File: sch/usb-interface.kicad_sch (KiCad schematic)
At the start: 4 parts, among them IC1 USB2244I-AEZG-06

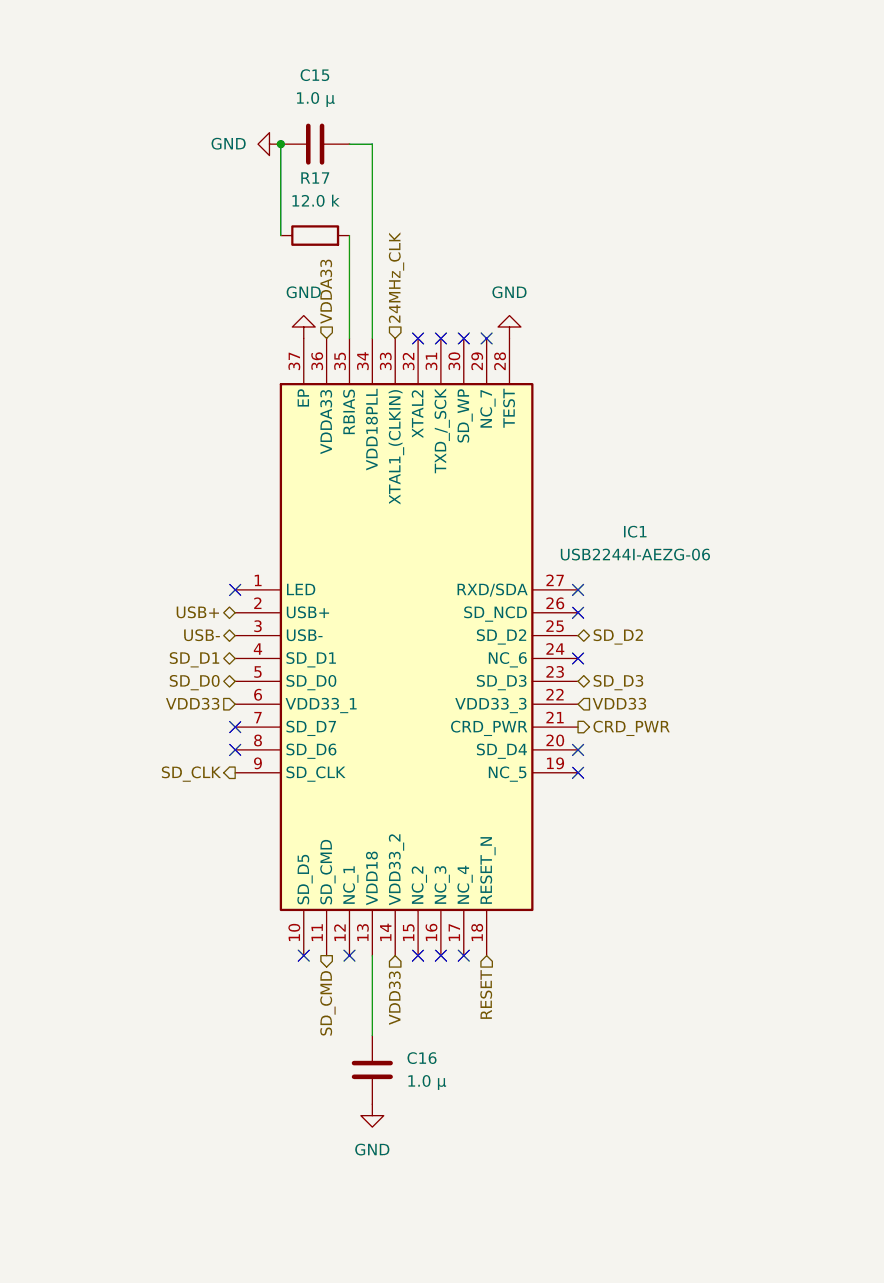
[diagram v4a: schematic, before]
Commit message: added ports to powersupply
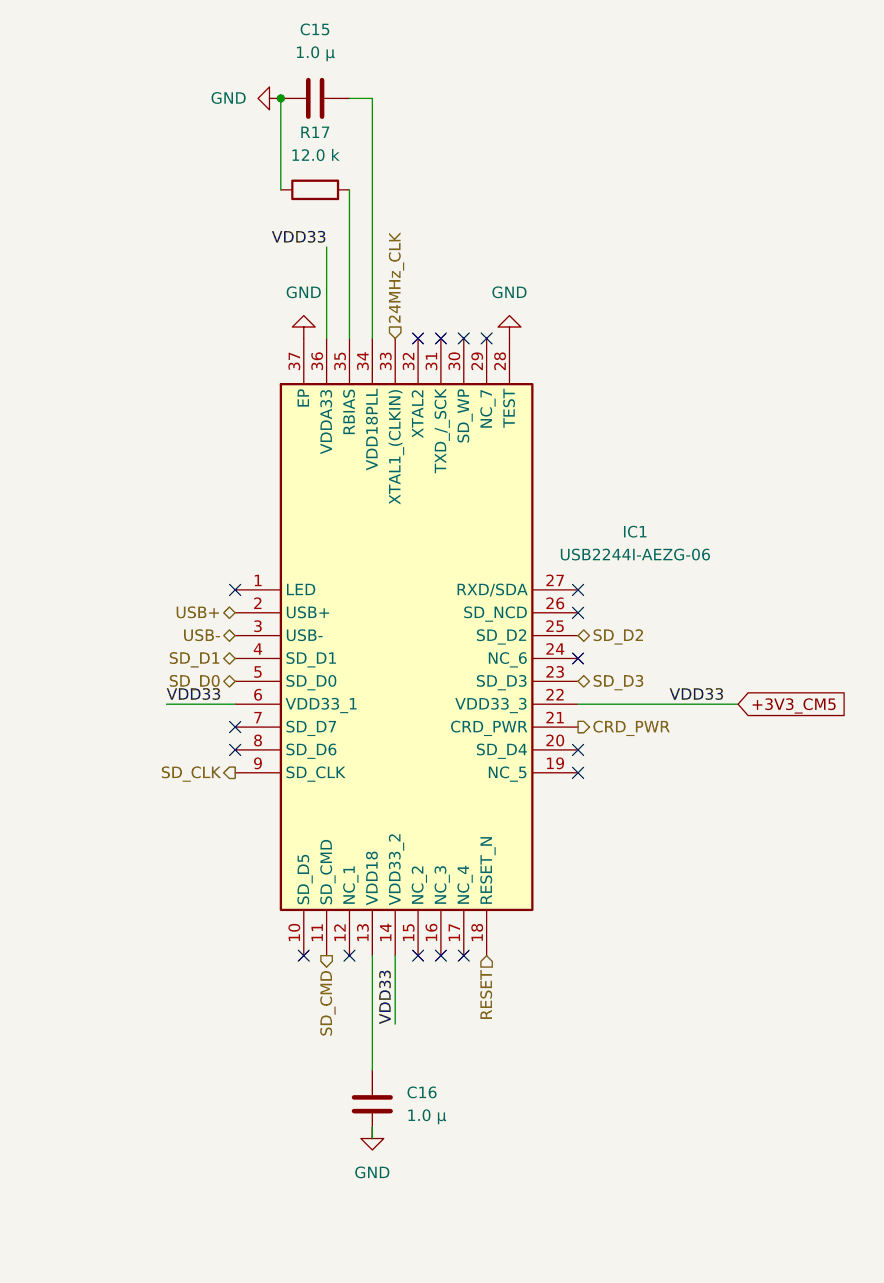
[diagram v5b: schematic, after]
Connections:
- net VDDA33 is gone; now on net +3V3_CM5: IC1.36 (VDDA33)
- net VDD33 renamed +3V3_CM5
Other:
- moved on the sheet: C15, C16, R17

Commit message: work pcb about 70 percent
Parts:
- added C21, C22, C23, C24: 4.7uF, Capacitor_SMD:C_0603_1608Metric, symbol Device:C_Small
- IC1: footprint QFN50P600X600X90-37N-D -> Package_DFN_QFN:QFN-36-1EP_6x6mm_P0.5mm_EP4.1x4.1mm_ThermalVias
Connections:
- net +3V3_CM5: now also C21.1, C22.1, C23.1, C24.2
- net GND: now also C21.2, C22.2, C23.2, C24.1
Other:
- moved on the sheet: C15, C16, R17

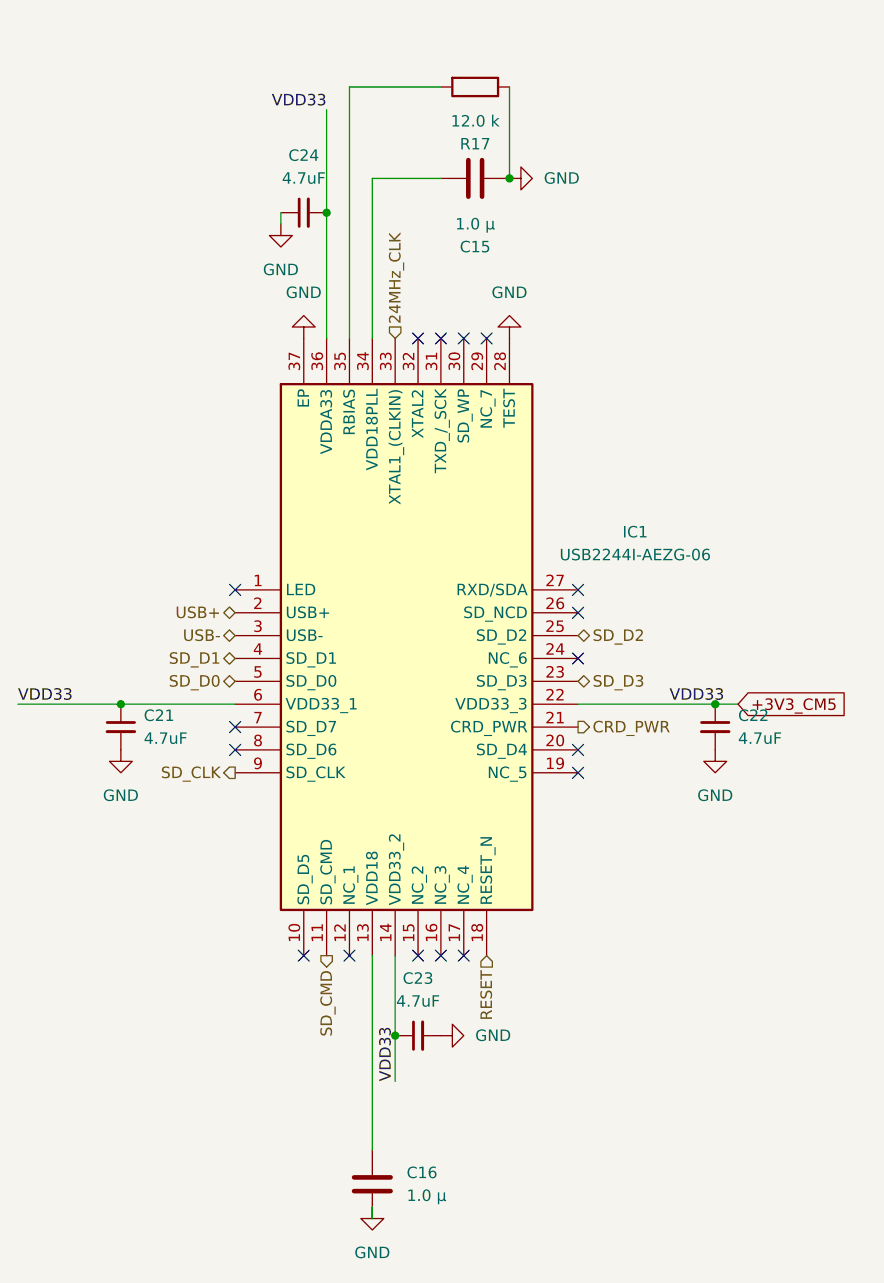
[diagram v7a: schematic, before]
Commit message: Endret nummereringer komponenter
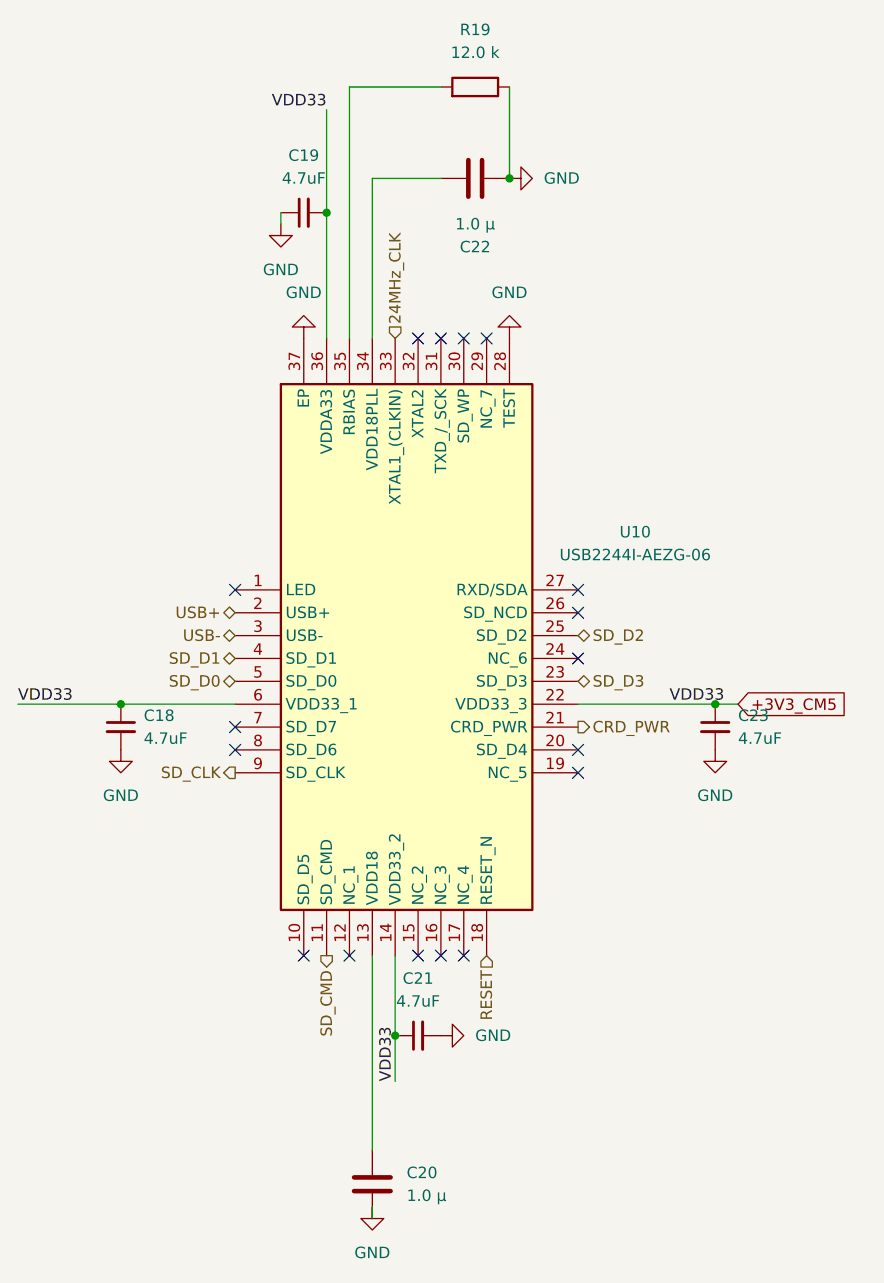
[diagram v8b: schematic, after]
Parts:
- renumbered C21 to C18, C24 to C19, C16 to C20, C23 to C21, C15 to C22, C22 to C23, R17 to R19, IC1 to U10
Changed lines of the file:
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@@
 		(dnp no)
 		(fields_autoplaced yes)
-		(property "Reference" "#PWR037"
+		(property "Reference" "#PWR066"
 			(at 55.88 109.22 0)
 			(effects
@@
 			(project "audiograb"
 				(path "/c46c2311-6d4b-411d-b012-c7730eac136d/53f9c81a-1433-4854-9dfc-932cf29aee40"
-					(reference "#PWR037")
+					(reference "#PWR066")
 					(unit 1)
 				)
@@
 		(dnp no)
 		(fields_autoplaced yes)
-		(property "Reference" "C22"
+		(property "Reference" "C23"
 			(at 124.46 99.0662 0)
 			(effects
@@
 			(project "audiograb"
 				(path "/c46c2311-6d4b-411d-b012-c7730eac136d/53f9c81a-1433-4854-9dfc-932cf29aee40"
-					(reference "C22")
+					(reference "C23")
 					(unit 1)
 				)
@@
 		(dnp no)
 		(fields_autoplaced yes)
-		(property "Reference" "C21"
+		(property "Reference" "C18"
 			(at 58.42 99.0662 0)
 			(effects
@@
 			(project "audiograb"
 				(path "/c46c2311-6d4b-411d-b012-c7730eac136d/53f9c81a-1433-4854-9dfc-932cf29aee40"
-					(reference "C21")
+					(reference "C18")
 					(unit 1)
 				)
@@
 		(dnp no)
 		(fields_autoplaced yes)
-		(property "Reference" "#PWR060"
+		(property "Reference" "#PWR069"
 			(at 83.82 160.02 0)
 			(effects
@@
 			(project "audiograb"
 				(path "/c46c2311-6d4b-411d-b012-c7730eac136d/53f9c81a-1433-4854-9dfc-932cf29aee40"
-					(reference "#PWR060")
+					(reference "#PWR069")
 					(unit 1)
 				)
@@
 		(dnp no)
 		(fields_autoplaced yes)
-		(property "Reference" "#PWR032"
+		(property "Reference" "#PWR070"
 			(at 97.79 134.62 0)
 			(effects
@@
 			(project "audiograb"
 				(path "/c46c2311-6d4b-411d-b012-c7730eac136d/53f9c81a-1433-4854-9dfc-932cf29aee40"
-					(reference "#PWR032")
+					(reference "#PWR070")
 					(unit 1)
 				)
@@
 		(dnp no)
 		(fields_autoplaced yes)
-		(property "Reference" "#PWR069"
+		(property "Reference" "#PWR067"
 			(at 73.66 50.8 0)
 			(effects
@@
 			(project "audiograb"
 				(path "/c46c2311-6d4b-411d-b012-c7730eac136d/53f9c81a-1433-4854-9dfc-932cf29aee40"
-					(reference "#PWR069")
+					(reference "#PWR067")
 					(unit 1)
 				)
@@
 		(dnp no)
 		(fields_autoplaced yes)
-		(property "Reference" "C15"
+		(property "Reference" "C22"
 			(at 95.25 46.99 90)
 			(effects
@@
 			(project "audiograb"
 				(path "/c46c2311-6d4b-411d-b012-c7730eac136d/53f9c81a-1433-4854-9dfc-932cf29aee40"
-					(reference "C15")
+					(reference "C22")
 					(unit 1)
 				)
@@
 		(dnp no)
 		(fields_autoplaced yes)
-		(property "Reference" "C24"
+		(property "Reference" "C19"
 			(at 76.2063 36.83 90)
 			(effects
@@
 			(project "audiograb"
 				(path "/c46c2311-6d4b-411d-b012-c7730eac136d/53f9c81a-1433-4854-9dfc-932cf29aee40"
-					(reference "C24")
+					(reference "C19")
 					(unit 1)
 				)
@@
 		(dnp no)
 		(fields_autoplaced yes)
-		(property "Reference" "C23"
+		(property "Reference" "C21"
 			(at 88.9063 128.27 90)
 			(effects
@@
 			(project "audiograb"
 				(path "/c46c2311-6d4b-411d-b012-c7730eac136d/53f9c81a-1433-4854-9dfc-932cf29aee40"
-					(reference "C23")
+					(reference "C21")
 					(unit 1)
 				)
@@
 		(dnp no)
 		(fields_autoplaced yes)
-		(property "Reference" "C16"
+		(property "Reference" "C20"
 			(at 87.63 149.8599 0)
 			(effects
@@
 			(project "audiograb"
 				(path "/c46c2311-6d4b-411d-b012-c7730eac136d/53f9c81a-1433-4854-9dfc-932cf29aee40"
-					(reference "C16")
+					(reference "C20")
 					(unit 1)
 				)
@@
 		(lib_id "Device:R")
 		(at 95.25 29.21 270)
-		(unit 1)
-		(exclude_from_sim no)
-		(in_bom yes)
-		(on_board yes)
-		(dnp no)
-		(fields_autoplaced yes)
-		(property "Reference" "R17"
-			(at 95.25 35.56 90)
+		(mirror x)
+		(unit 1)
+		(exclude_from_sim no)
+		(in_bom yes)
+		(on_board yes)
+		(dnp no)
+		(property "Reference" "R19"
+			(at 95.25 22.86 90)
 			(effects
 				(font
@@
 		)
 		(property "Value" "12.0 k"
-			(at 95.25 33.02 90)
+			(at 95.25 25.4 90)
 			(effects
 				(font
@@
 		)
 		(property "Footprint" "Resistor_SMD:R_0603_1608Metric"
-			(at 95.25 27.432 90)
+			(at 95.25 30.988 90)
 			(effects
 				(font
@@
 			(project "audiograb"
 				(path "/c46c2311-6d4b-411d-b012-c7730eac136d/53f9c81a-1433-4854-9dfc-932cf29aee40"
-					(reference "R17")
+					(reference "R19")
 					(unit 1)
 				)
@@
 		(dnp no)
 		(fields_autoplaced yes)
-		(property "Reference" "#PWR061"
+		(property "Reference" "#PWR072"
 			(at 99.06 50.8 0)
 			(effects
@@
 			(project "audiograb"
 				(path "/c46c2311-6d4b-411d-b012-c7730eac136d/53f9c81a-1433-4854-9dfc-932cf29aee40"
-					(reference "#PWR061")
+					(reference "#PWR072")
 					(unit 1)
 				)
@@
 		(dnp no)
 		(fields_autoplaced yes)
-		(property "Reference" "#PWR034"
+		(property "Reference" "#PWR073"
 			(at 121.92 109.22 0)
 			(effects
@@
 			(project "audiograb"
 				(path "/c46c2311-6d4b-411d-b012-c7730eac136d/53f9c81a-1433-4854-9dfc-932cf29aee40"
-					(reference "#PWR034")
+					(reference "#PWR073")
 					(unit 1)
 				)
@@
 		(on_board yes)
 		(dnp no)
-		(property "Reference" "#PWR059"
+		(property "Reference" "#PWR068"
 			(at 76.2 50.8 0)
 			(effects
@@
 			(project "audiograb"
 				(path "/c46c2311-6d4b-411d-b012-c7730eac136d/53f9c81a-1433-4854-9dfc-932cf29aee40"
-					(reference "#PWR059")
+					(reference "#PWR068")
 					(unit 1)
 				)
@@
 		(dnp no)
 		(fields_autoplaced yes)
-		(property "Reference" "#PWR058"
+		(property "Reference" "#PWR071"
 			(at 105.41 39.37 0)
 			(effects
@@
 			(project "audiograb"
 				(path "/c46c2311-6d4b-411d-b012-c7730eac136d/53f9c81a-1433-4854-9dfc-932cf29aee40"
-					(reference "#PWR058")
+					(reference "#PWR071")
 					(unit 1)
 				)
@@
 		(dnp no)
 		(fields_autoplaced yes)
-		(property "Reference" "IC1"
+		(property "Reference" "U10"
 			(at 113.03 78.6698 0)
 			(effects
@@
 			(project "audiograb"
 				(path "/c46c2311-6d4b-411d-b012-c7730eac136d/53f9c81a-1433-4854-9dfc-932cf29aee40"
-					(reference "IC1")
-					(unit 1)
-				)
+					(reference "U10")
+					(unit 1)
+				)
